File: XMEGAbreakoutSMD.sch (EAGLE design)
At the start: 22 parts, among them IC1 XMEGA16A4

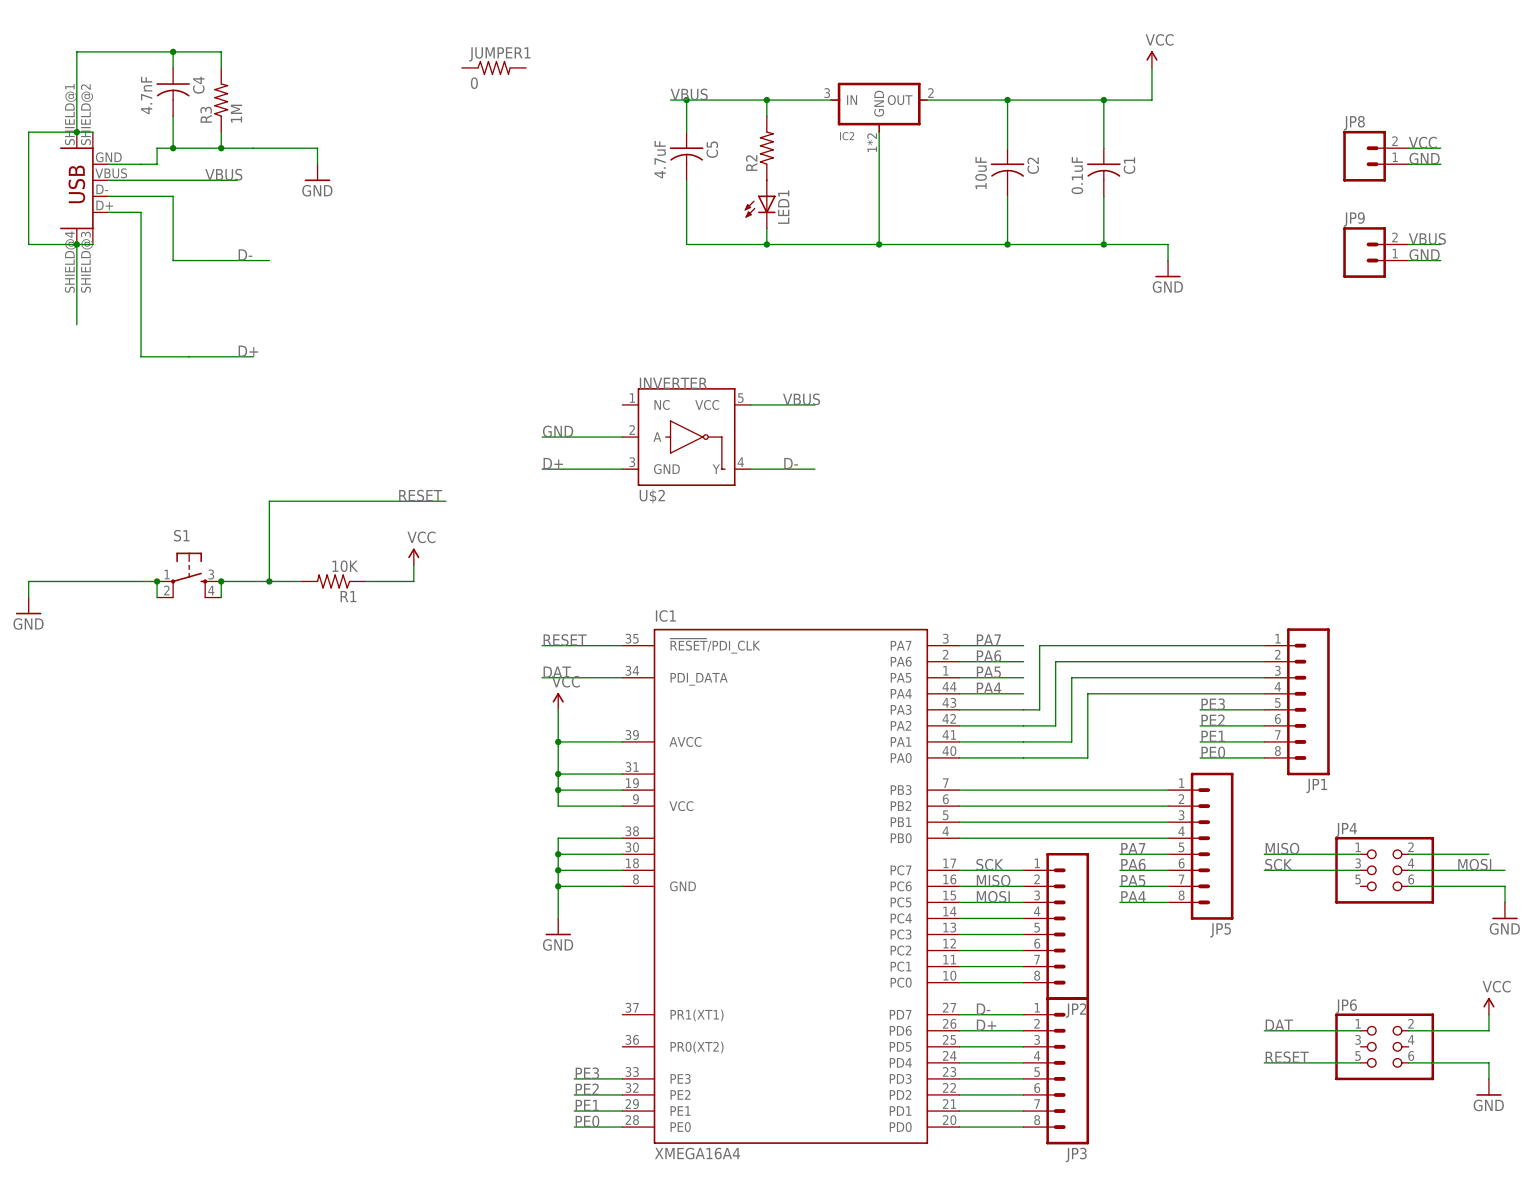
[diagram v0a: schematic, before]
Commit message: d+ and d- switched
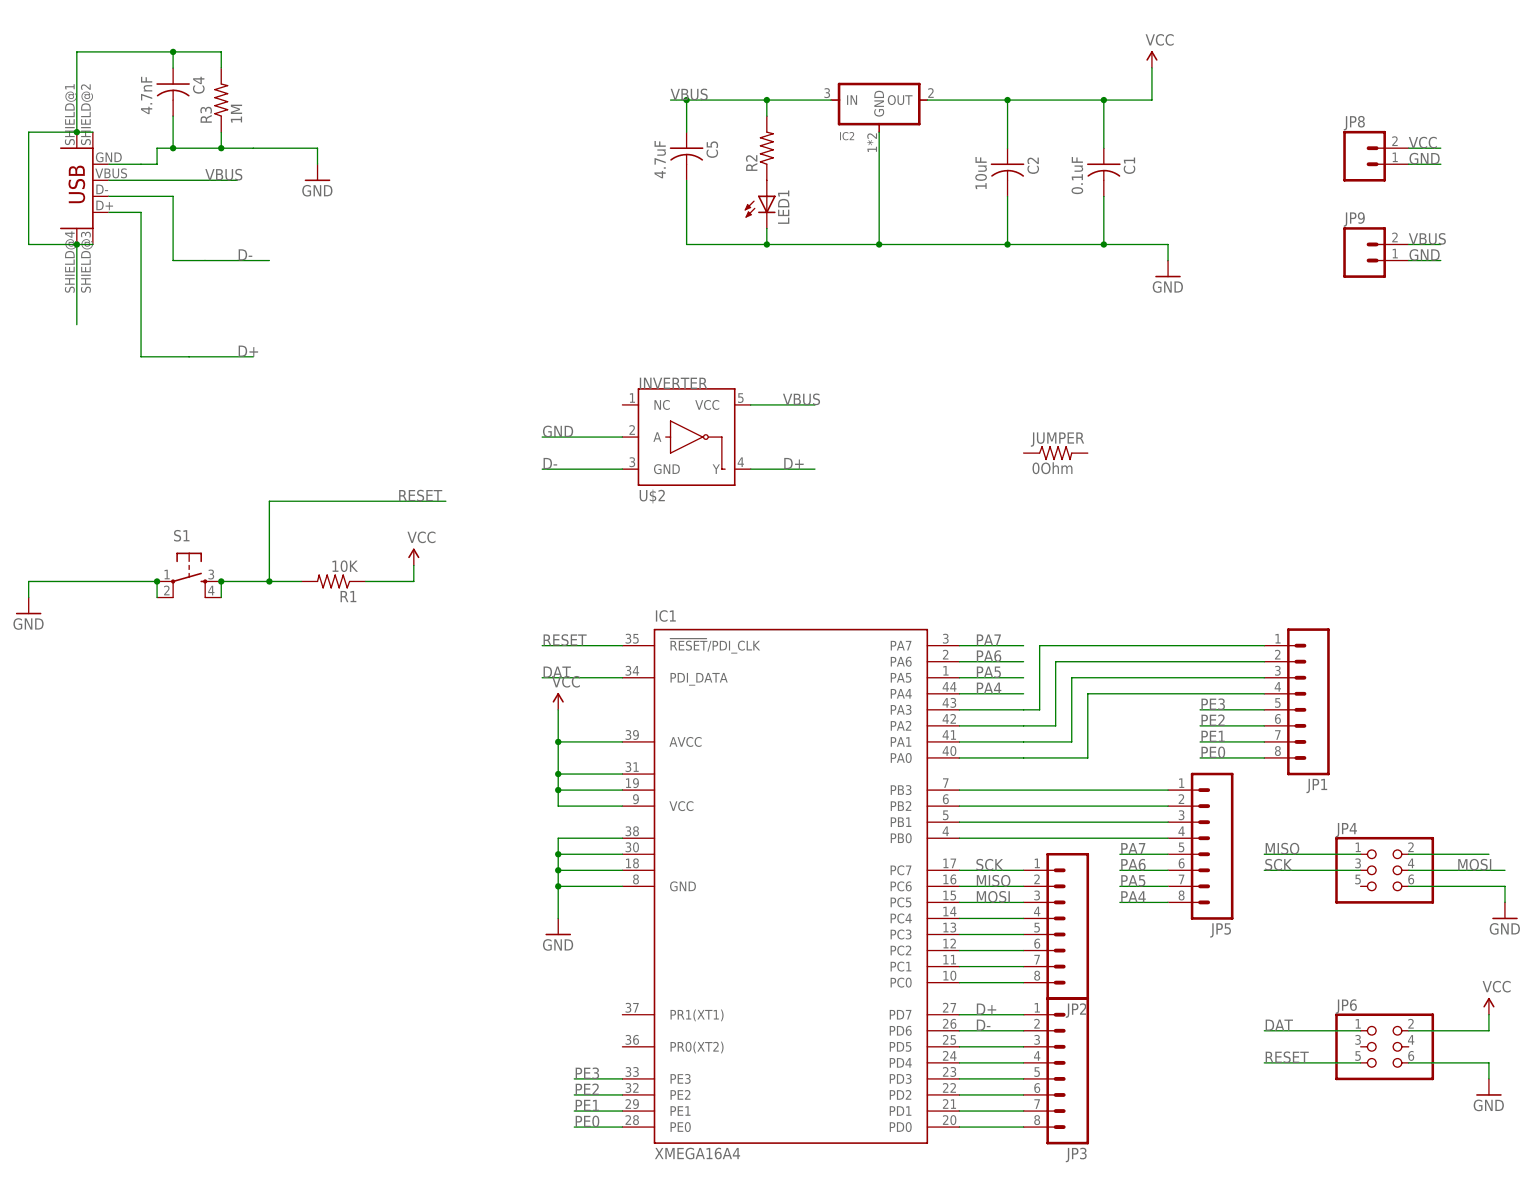
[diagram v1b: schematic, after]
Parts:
- removed JUMPER1: 0, fab:RES-US1206FAB
- added JUMPER: 0Ohm, fab:RES-US1206FAB
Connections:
- net D+: now also IC1.PD7, JP3.1, U$2.Y; no longer IC1.PD6, JP3.2, U$2.GND
- net D-: now also IC1.PD6, JP3.2, U$2.GND; no longer IC1.PD7, JP3.1, U$2.Y
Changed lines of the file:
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@@
 <part name="P+4" library="SparkFun" deviceset="VCC" device=""/>
 <part name="GND5" library="SparkFun" deviceset="GND" device=""/>
-<part name="JUMPER1" library="fab" deviceset="RES-US" device="1206FAB" value="0"/>
 <part name="C5" library="fab" deviceset="CAP-US" device="1206" value="4.7uF"/>
 <part name="U$2" library="SparkFun" deviceset="INVERTER" device=""/>
@@
 <part name="GND6" library="SparkFun" deviceset="GND" device=""/>
 <part name="P+2" library="SparkFun" deviceset="VCC" device=""/>
+<part name="JUMPER" library="fab" deviceset="RES-US" device="1206FAB" value="0Ohm"/>
 </parts>
 <sheets>
@@
 <instance part="P+4" gate="1" x="104.14" y="175.26"/>
 <instance part="GND5" gate="1" x="106.68" y="142.24"/>
-<instance part="JUMPER1" gate="G$1" x="0" y="175.26"/>
 <instance part="C5" gate="G$1" x="30.48" y="162.56" rot="R270"/>
 <instance part="U$2" gate="G$1" x="30.48" y="116.84"/>
@@
 <instance part="GND6" gate="1" x="157.48" y="12.7"/>
 <instance part="P+2" gate="1" x="157.48" y="25.4"/>
+<instance part="JUMPER" gate="G$1" x="88.9" y="114.3"/>
 </instances>
 <busses>
@@
 <net name="D+" class="0">
 <segment>
-<pinref part="IC1" gate="G$1" pin="PD6"/>
-<pinref part="JP3" gate="G$1" pin="2"/>
-<wire x1="73.66" y1="22.86" x2="83.82" y2="22.86" width="0.1524" layer="91"/>
-<label x="76.2" y="22.86" size="1.778" layer="95"/>
-</segment>
-<segment>
 <pinref part="U$1" gate="G$1" pin="D+"/>
 <wire x1="-60.96" y1="152.4" x2="-55.88" y2="152.4" width="0.1524" layer="91"/>
@@
 </segment>
 <segment>
-<pinref part="U$2" gate="G$1" pin="GND"/>
-<wire x1="20.32" y1="111.76" x2="7.62" y2="111.76" width="0.1524" layer="91"/>
-<label x="7.62" y="111.76" size="1.778" layer="95"/>
+<pinref part="IC1" gate="G$1" pin="PD7"/>
+<pinref part="JP3" gate="G$1" pin="1"/>
+<wire x1="73.66" y1="25.4" x2="83.82" y2="25.4" width="0.1524" layer="91"/>
+<label x="76.2" y="25.4" size="1.778" layer="95"/>
+</segment>
+<segment>
+<pinref part="U$2" gate="G$1" pin="Y"/>
+<wire x1="40.64" y1="111.76" x2="50.8" y2="111.76" width="0.1524" layer="91"/>
+<label x="45.72" y="111.76" size="1.778" layer="95"/>
 </segment>
 </net>
@@
 </segment>
 <segment>
-<pinref part="IC1" gate="G$1" pin="PD7"/>
-<pinref part="JP3" gate="G$1" pin="1"/>
-<wire x1="73.66" y1="25.4" x2="83.82" y2="25.4" width="0.1524" layer="91"/>
-<label x="76.2" y="25.4" size="1.778" layer="95"/>
-</segment>
-<segment>
-<pinref part="U$2" gate="G$1" pin="Y"/>
-<wire x1="40.64" y1="111.76" x2="50.8" y2="111.76" width="0.1524" layer="91"/>
-<label x="45.72" y="111.76" size="1.778" layer="95"/>
-</segment>
-</net>
+<pinref part="IC1" gate="G$1" pin="PD6"/>
+<pinref part="JP3" gate="G$1" pin="2"/>
+<wire x1="73.66" y1="22.86" x2="83.82" y2="22.86" width="0.1524" layer="91"/>
+<label x="76.2" y="22.86" size="1.778" layer="95"/>
+</segment>
+<segment>
+<pinref part="U$2" gate="G$1" pin="GND"/>
+<wire x1="20.32" y1="111.76" x2="7.62" y2="111.76" width="0.1524" layer="91"/>
+<label x="7.62" y="111.76" size="1.778" layer="95"/>
+</segment>
+</net>

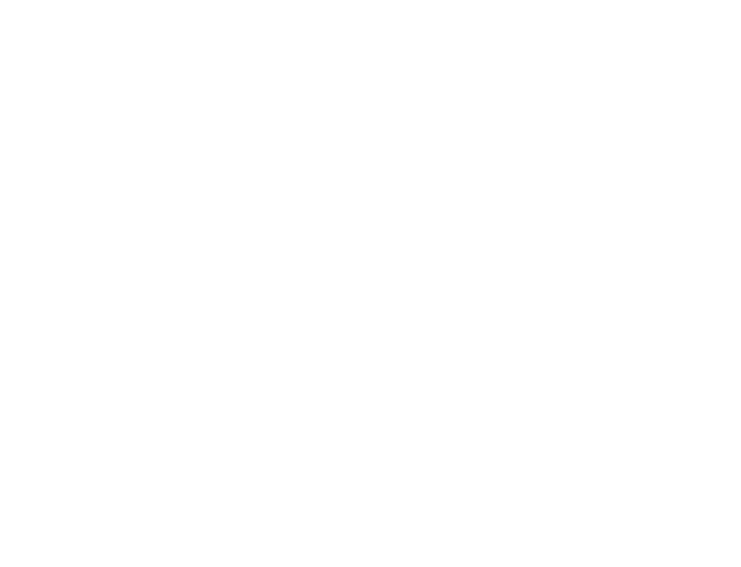
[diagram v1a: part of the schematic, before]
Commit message: solder jumper on 5V
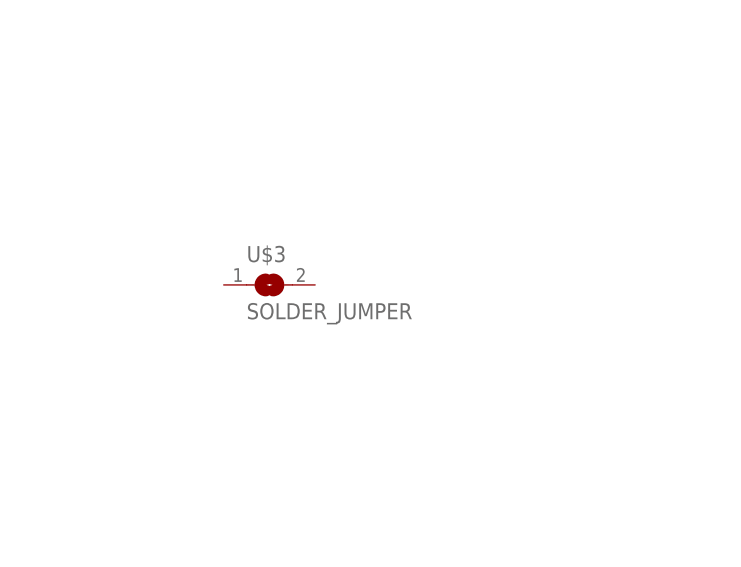
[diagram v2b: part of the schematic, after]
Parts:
- added U$3: SOLDER_JUMPER, fab:SOLDER_JUMPER
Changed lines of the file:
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@@
 <part name="P+2" library="SparkFun" deviceset="VCC" device=""/>
 <part name="JUMPER" library="fab" deviceset="RES-US" device="1206FAB" value="0Ohm"/>
+<part name="U$3" library="fab" deviceset="SOLDER_JUMPER" device=""/>
 </parts>
 <sheets>
@@
 <instance part="P+2" gate="1" x="157.48" y="25.4"/>
 <instance part="JUMPER" gate="G$1" x="88.9" y="114.3"/>
+<instance part="U$3" gate="G$1" x="-48.26" y="40.64"/>
 </instances>
 <busses>

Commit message: smd
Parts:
- added C3: 0.1uF, fab:CAP-US1206FAB
- added C6, C7: 0.1uF, fab:CAP-US1206
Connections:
- net GND: now also C3.2, C6.2, C7.2
- net VCC: now also C3.1, C6.1, C7.1
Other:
- moved on the sheet: C1, C2, C5, IC2, LED1, R2, U$3
